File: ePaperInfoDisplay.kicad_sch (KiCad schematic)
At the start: 52 parts, among them J1 Conn_01x02_Pin, J2 USB_C_Receptacle_USB2.0, Q1 Q_NMOS_GSD, Q2 Q_PMOS_GSD, Q3 Q_PMOS_GSD, SW1 SW_Push, SW2 SW_Push, U1 MCP73831-2-OT, U2 MIC5219-3.3YM5, U3 ePD_iTC

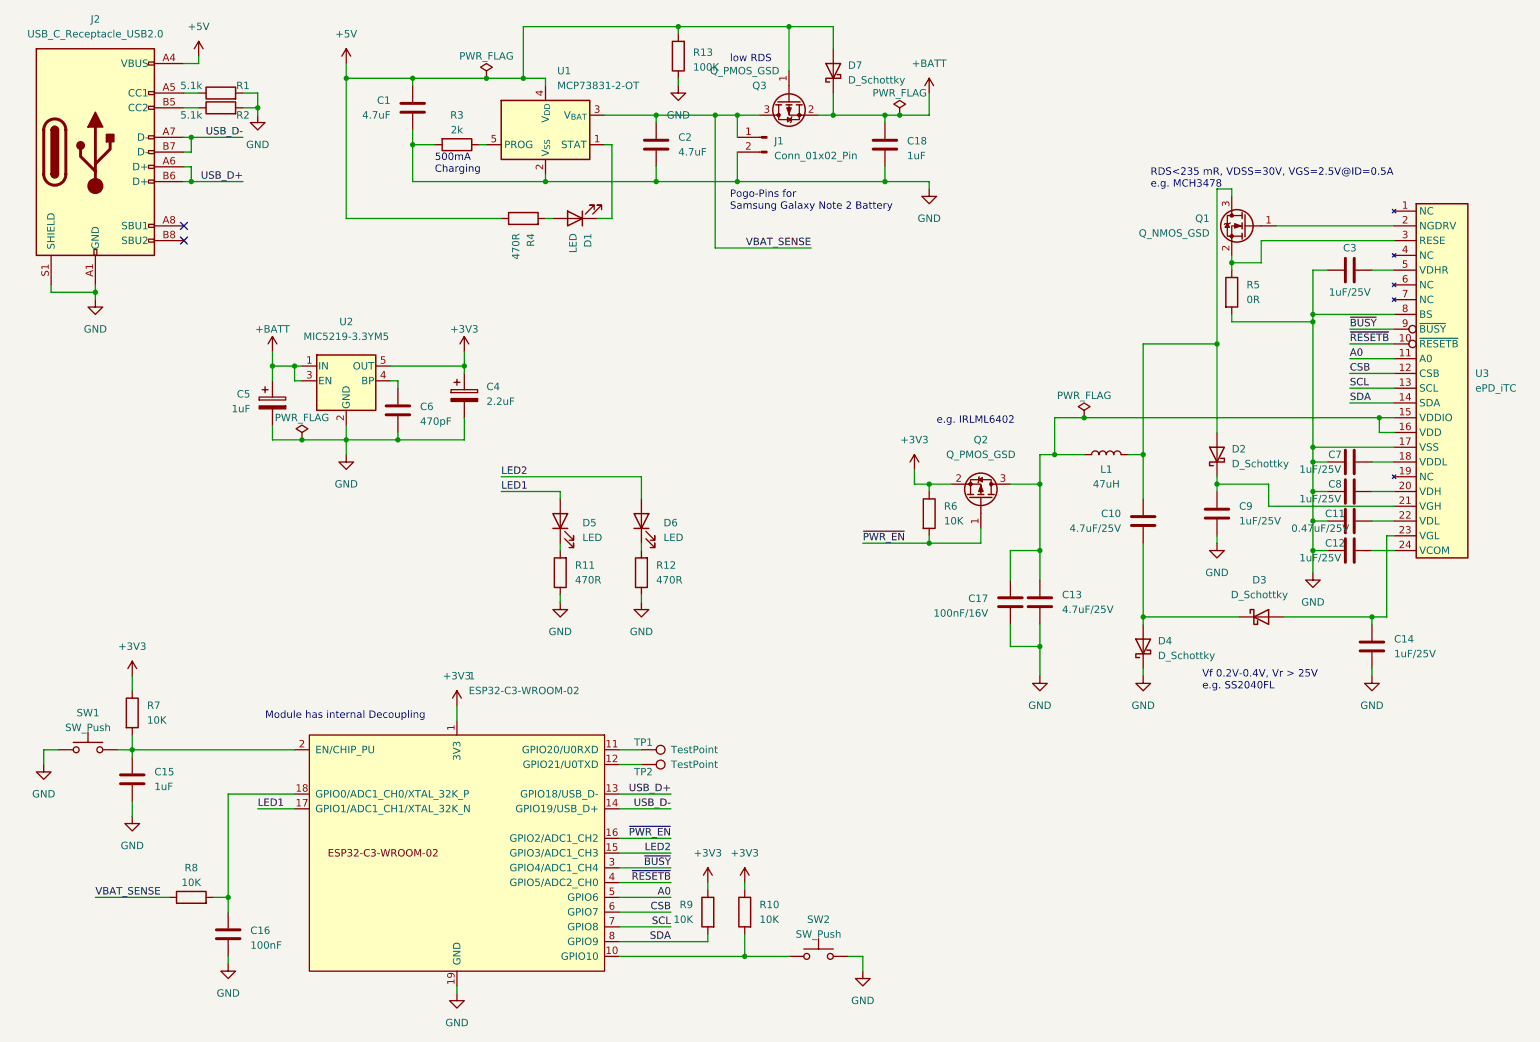
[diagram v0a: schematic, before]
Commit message: Add Revision 2
Use Bottom-connect FPC connector, mirror some parts of the layout
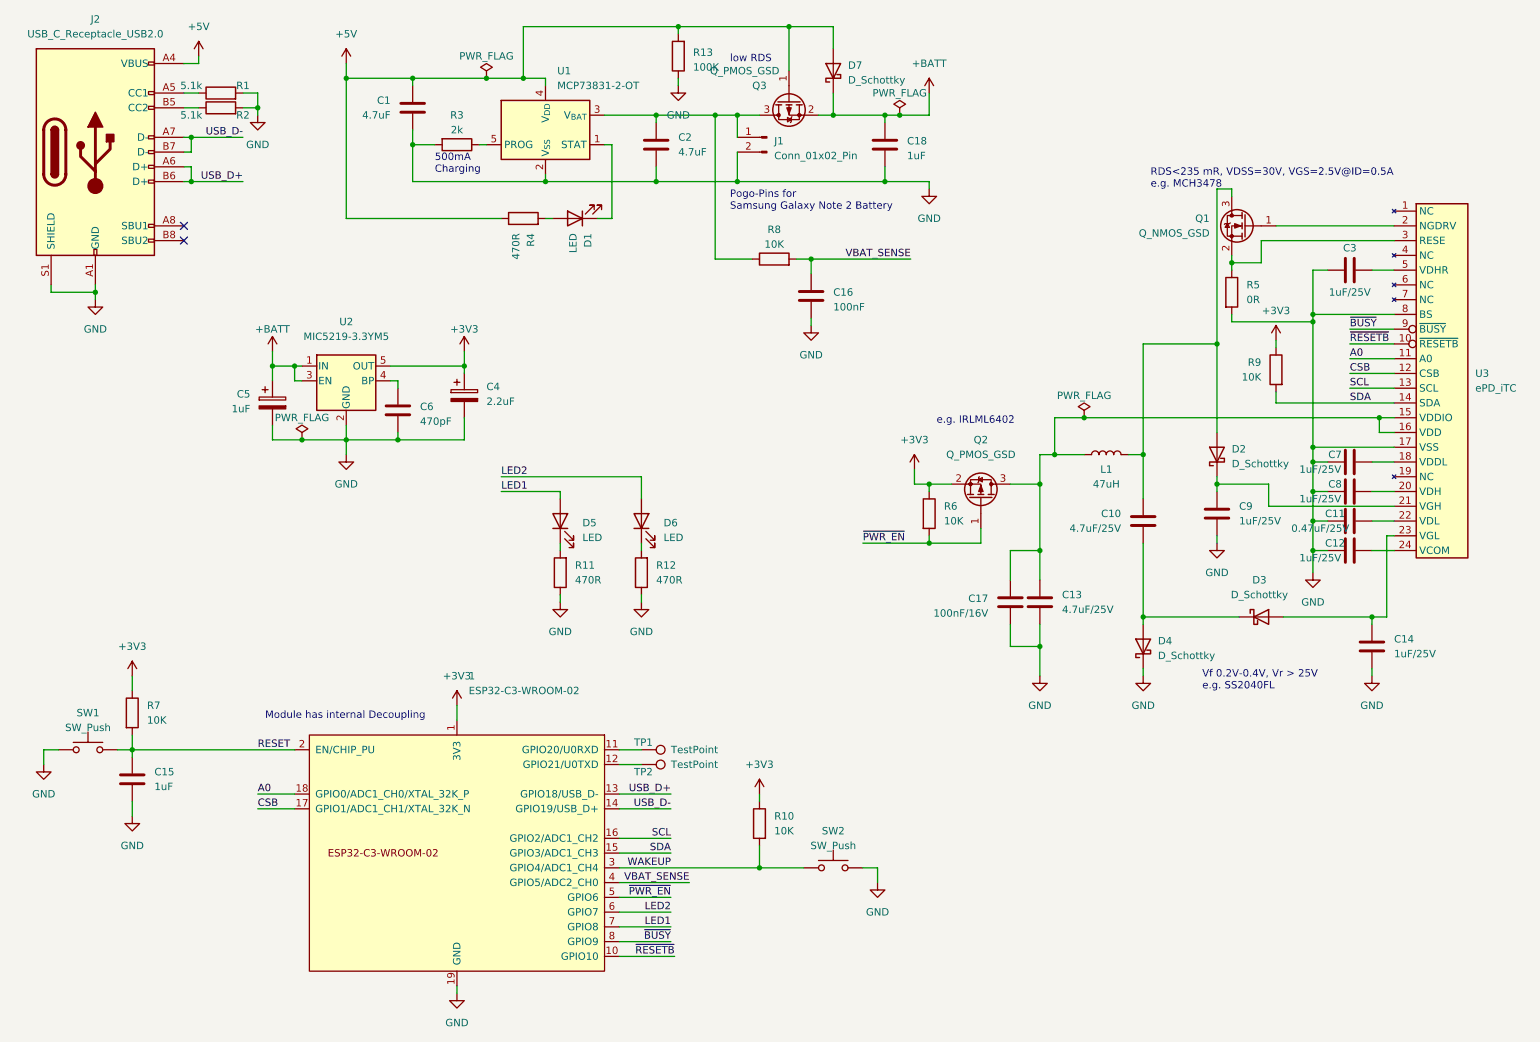
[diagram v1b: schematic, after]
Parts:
- U3: footprint Connector_FFC-FPC:TE_2-1734839-4_1x24-1MP_P0.5mm_Horizontal -> nr-lib:TE_2-1734592-4_1x24-1MP_P0.5mm_Horizontal
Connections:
- net A0: now also 1.18 (GPIO0/ADC1_CH0/XTAL_32K_P); no longer 1.5 (GPIO6)
- net CSB: now also 1.17 (GPIO1/ADC1_CH1/XTAL_32K_N); no longer 1.6 (GPIO7)
- net LED1: now also 1.7 (GPIO8); no longer 1.17 (GPIO1/ADC1_CH1/XTAL_32K_N)
- net LED2: now also 1.6 (GPIO7); no longer 1.15 (GPIO3/ADC1_CH3)
- net SCL: now also 1.16 (GPIO2/ADC1_CH2); no longer 1.7 (GPIO8)
- net SDA: now also 1.15 (GPIO3/ADC1_CH3); no longer 1.8 (GPIO9)
- net VBAT_SENSE: now also 1.4 (GPIO5/ADC2_CH0), C16.1, R8.2; no longer C2.1, J1.1 (Pin_1), Q3.3 (D), R8.1, U1.3 (V_{BAT})
- net ~{BUSY}: now also 1.8 (GPIO9); no longer 1.3 (GPIO4/ADC1_CH4)
- net ~{PWR_EN}: now also 1.5 (GPIO6); no longer 1.16 (GPIO2/ADC1_CH2)
- net ~{RESETB}: now also 1.10 (GPIO10); no longer 1.4 (GPIO5/ADC2_CH0)
- net WAKEUP: now reaches R10.2, SW2.2
- net WAKEUP: now also 1.3 (GPIO4/ADC1_CH4); no longer 1.10 (GPIO10)
- net RESET: now reaches 1.2 (EN/CHIP_PU), C15.1, R7.2, SW1.2
- new net: C2.1, J1.1 (Pin_1), Q3.3 (D), R8.1, U1.3 (V_{BAT})
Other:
- moved on the sheet: C16, R10, R8, R9, SW2
